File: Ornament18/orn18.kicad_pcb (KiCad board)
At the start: 2 copper layers, 50 x 50 mm, 15 parts, among them SW1 SW_Push, U1 ATTINY13A-SSU, U2 74LS138

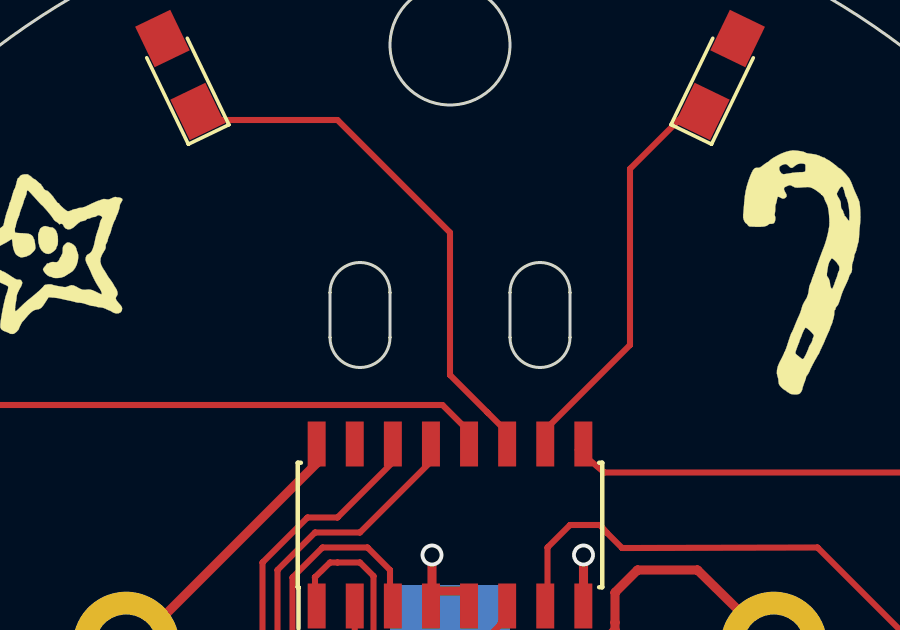
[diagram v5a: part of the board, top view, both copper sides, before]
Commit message: change mechanical holes to round from oval
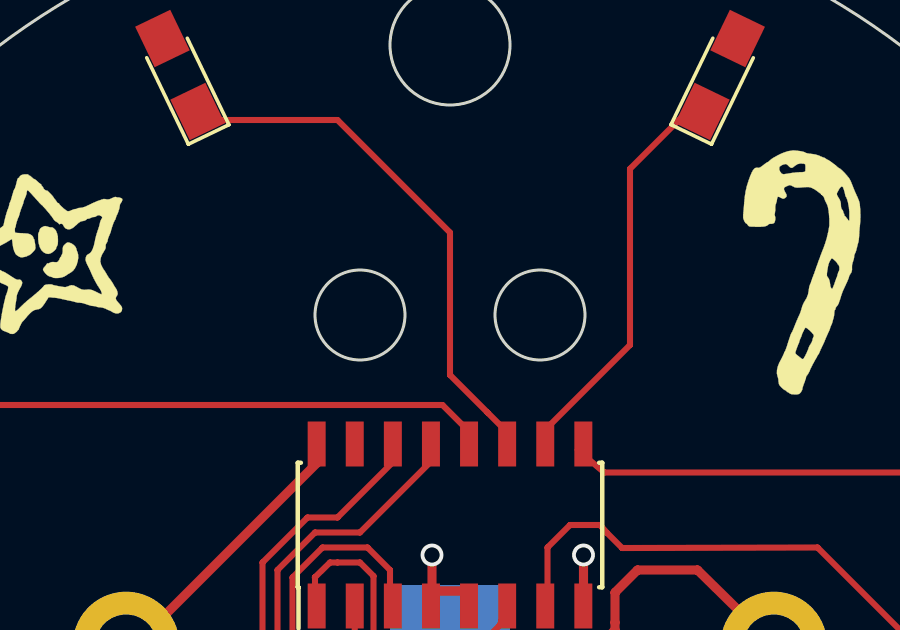
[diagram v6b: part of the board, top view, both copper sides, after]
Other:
- outline, holes or cut-outs redrawn
